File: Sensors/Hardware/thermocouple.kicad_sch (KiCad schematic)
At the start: 8 parts, among them U7 MAX31856

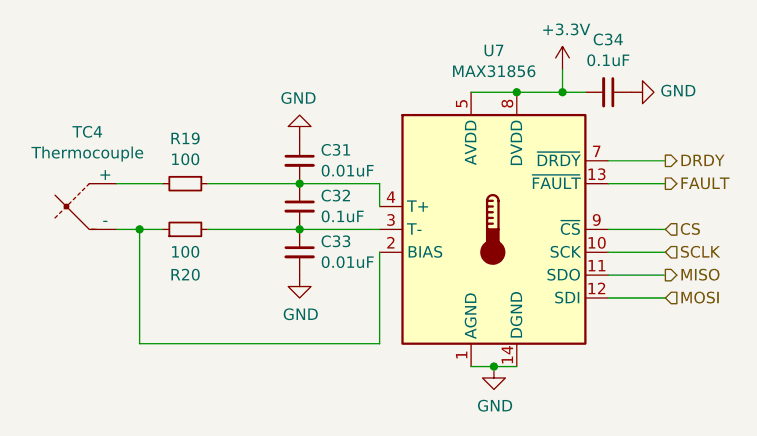
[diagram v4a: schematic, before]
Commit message: added 10V rail, moved to boosts sheet
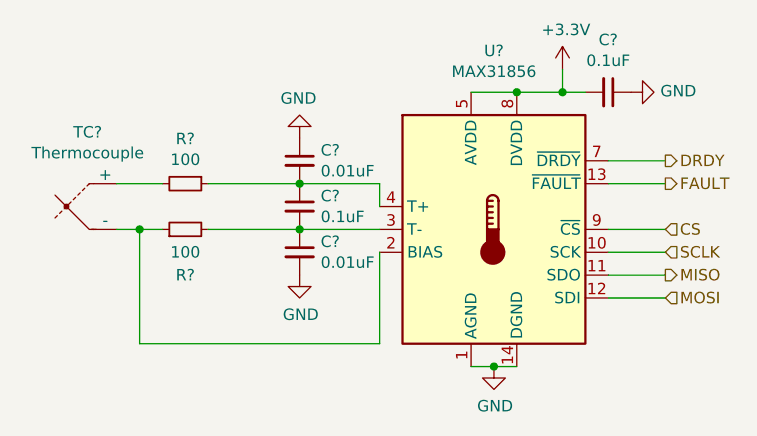
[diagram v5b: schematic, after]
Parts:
- renumbered C34 to C?, C32 to C?, C31 to C?, C33 to C?, R19 to R?, R20 to R?, TC4 to TC?, U7 to U?
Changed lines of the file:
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@@
   (symbol (lib_id "Sensor_Temperature:MAX31856") (at 95.25 73.66 0)
     (in_bom yes) (on_board yes)
-    (property "Reference" "U7" (id 0) (at 95.25 53.8226 0))
+    (property "Reference" "U?" (id 0) (at 95.25 53.8226 0))
     (property "Value" "MAX31856" (id 1) (at 95.25 56.134 0))
     (property "Footprint" "Package_SO:TSSOP-14_4.4x5mm_P0.65mm" (id 2) (at 99.06 87.63 0)
@@
   (symbol (lib_id "power:GND") (at 95.25 88.9 0)
     (in_bom yes) (on_board yes)
-    (property "Reference" "#PWR053" (id 0) (at 95.25 95.25 0)
+    (property "Reference" "#PWR?" (id 0) (at 95.25 95.25 0)
       (effects (font (size 1.27 1.27)) hide)
     )
@@
   (symbol (lib_id "analogue-cache:+3.3V") (at 102.87 55.88 0)
     (in_bom yes) (on_board yes)
-    (property "Reference" "#PWR054" (id 0) (at 102.87 59.69 0)
+    (property "Reference" "#PWR?" (id 0) (at 102.87 59.69 0)
       (effects (font (size 1.27 1.27)) hide)
     )
@@
   (symbol (lib_id "Device:C_Small") (at 107.95 58.42 270)
     (in_bom yes) (on_board yes)
-    (property "Reference" "C34" (id 0) (at 107.95 52.6034 90))
+    (property "Reference" "C?" (id 0) (at 107.95 52.6034 90))
     (property "Value" "0.1uF" (id 1) (at 107.95 54.9148 90))
     (property "Footprint" "Capacitor_SMD:C_0603_1608Metric" (id 2) (at 107.95 58.42 0)
@@
   (symbol (lib_id "power:GND") (at 110.49 58.42 90)
     (in_bom yes) (on_board yes)
-    (property "Reference" "#PWR055" (id 0) (at 116.84 58.42 0)
+    (property "Reference" "#PWR?" (id 0) (at 116.84 58.42 0)
       (effects (font (size 1.27 1.27)) hide)
     )
@@
   (symbol (lib_id "Device:Thermocouple") (at 50.8 71.12 0)
     (in_bom yes) (on_board yes)
-    (property "Reference" "TC4" (id 0) (at 50.1142 62.865 0))
+    (property "Reference" "TC?" (id 0) (at 50.1142 62.865 0))
     (property "Value" "Thermocouple" (id 1) (at 50.1142 65.1764 0))
     (property "Footprint" "TerminalBlock_TE-Connectivity:TerminalBlock_TE_282834-2_1x02_P2.54mm_Horizontal" (id 2) (at 36.195 69.85 0)
@@
   (symbol (lib_id "Device:R_Small") (at 60.96 68.58 270)
     (in_bom yes) (on_board yes)
-    (property "Reference" "R19" (id 0) (at 60.96 63.6016 90))
+    (property "Reference" "R?" (id 0) (at 60.96 63.6016 90))
     (property "Value" "100" (id 1) (at 60.96 65.913 90))
     (property "Footprint" "Resistor_SMD:R_0603_1608Metric" (id 2) (at 60.96 68.58 0)
@@
   (symbol (lib_id "Device:R_Small") (at 60.96 73.66 90)
     (in_bom yes) (on_board yes)
-    (property "Reference" "R20" (id 0) (at 60.96 78.74 90))
+    (property "Reference" "R?" (id 0) (at 60.96 78.74 90))
     (property "Value" "100" (id 1) (at 60.96 76.2 90))
     (property "Footprint" "Resistor_SMD:R_0603_1608Metric" (id 2) (at 60.96 73.66 0)
@@
   (symbol (lib_id "Device:C_Small") (at 73.66 71.12 0)
     (in_bom yes) (on_board yes)
-    (property "Reference" "C32" (id 0) (at 75.9968 69.9516 0)
+    (property "Reference" "C?" (id 0) (at 75.9968 69.9516 0)
       (effects (font (size 1.27 1.27)) (justify left))
     )
@@
   (symbol (lib_id "Device:C_Small") (at 73.66 66.04 0)
     (in_bom yes) (on_board yes)
-    (property "Reference" "C31" (id 0) (at 75.9968 64.8716 0)
+    (property "Reference" "C?" (id 0) (at 75.9968 64.8716 0)
       (effects (font (size 1.27 1.27)) (justify left))
     )
@@
   (symbol (lib_id "Device:C_Small") (at 73.66 76.2 0)
     (in_bom yes) (on_board yes)
-    (property "Reference" "C33" (id 0) (at 75.9968 75.0316 0)
+    (property "Reference" "C?" (id 0) (at 75.9968 75.0316 0)
       (effects (font (size 1.27 1.27)) (justify left))
     )
@@
   (symbol (lib_id "power:GND") (at 73.66 78.74 0)
     (in_bom yes) (on_board yes)
-    (property "Reference" "#PWR052" (id 0) (at 73.66 85.09 0)
+    (property "Reference" "#PWR?" (id 0) (at 73.66 85.09 0)
       (effects (font (size 1.27 1.27)) hide)
     )
@@
   (symbol (lib_id "power:GND") (at 73.66 63.5 180)
     (in_bom yes) (on_board yes)
-    (property "Reference" "#PWR051" (id 0) (at 73.66 57.15 0)
+    (property "Reference" "#PWR?" (id 0) (at 73.66 57.15 0)
       (effects (font (size 1.27 1.27)) hide)
     )

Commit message: fp assignments
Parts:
- C19, C20, C21, C22: renamed from C?; footprint Capacitor_SMD:C_0603_1608Metric -> Capacitor_SMD:C_0402_1005Metric
- R10, R11: renamed from R?; footprint Resistor_SMD:R_0603_1608Metric -> Resistor_SMD:R_0402_1005Metric
- gave numbers to parts that had none: 2
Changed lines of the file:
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@@
   (symbol (lib_id "Sensor_Temperature:MAX31856") (at 95.25 73.66 0)
     (in_bom yes) (on_board yes)
-    (property "Reference" "U?" (id 0) (at 95.25 53.8226 0))
+    (property "Reference" "U3" (id 0) (at 95.25 53.8226 0))
     (property "Value" "MAX31856" (id 1) (at 95.25 56.134 0))
     (property "Footprint" "Package_SO:TSSOP-14_4.4x5mm_P0.65mm" (id 2) (at 99.06 87.63 0)
@@
   (symbol (lib_id "power:GND") (at 95.25 88.9 0)
     (in_bom yes) (on_board yes)
-    (property "Reference" "#PWR?" (id 0) (at 95.25 95.25 0)
+    (property "Reference" "#PWR034" (id 0) (at 95.25 95.25 0)
       (effects (font (size 1.27 1.27)) hide)
     )
@@
   (symbol (lib_id "analogue-cache:+3.3V") (at 102.87 55.88 0)
     (in_bom yes) (on_board yes)
-    (property "Reference" "#PWR?" (id 0) (at 102.87 59.69 0)
+    (property "Reference" "#PWR035" (id 0) (at 102.87 59.69 0)
       (effects (font (size 1.27 1.27)) hide)
     )
@@
   (symbol (lib_id "Device:C_Small") (at 107.95 58.42 270)
     (in_bom yes) (on_board yes)
-    (property "Reference" "C?" (id 0) (at 107.95 52.6034 90))
+    (property "Reference" "C22" (id 0) (at 107.95 52.6034 90))
     (property "Value" "0.1uF" (id 1) (at 107.95 54.9148 90))
-    (property "Footprint" "Capacitor_SMD:C_0603_1608Metric" (id 2) (at 107.95 58.42 0)
+    (property "Footprint" "Capacitor_SMD:C_0402_1005Metric" (id 2) (at 107.95 58.42 0)
       (effects (font (size 1.27 1.27)) hide)
     )
@@
   (symbol (lib_id "power:GND") (at 110.49 58.42 90)
     (in_bom yes) (on_board yes)
-    (property "Reference" "#PWR?" (id 0) (at 116.84 58.42 0)
+    (property "Reference" "#PWR036" (id 0) (at 116.84 58.42 0)
       (effects (font (size 1.27 1.27)) hide)
     )
@@
   (symbol (lib_id "Device:Thermocouple") (at 50.8 71.12 0)
     (in_bom yes) (on_board yes)
-    (property "Reference" "TC?" (id 0) (at 50.1142 62.865 0))
+    (property "Reference" "TC2" (id 0) (at 50.1142 62.865 0))
     (property "Value" "Thermocouple" (id 1) (at 50.1142 65.1764 0))
     (property "Footprint" "TerminalBlock_TE-Connectivity:TerminalBlock_TE_282834-2_1x02_P2.54mm_Horizontal" (id 2) (at 36.195 69.85 0)
@@
   (symbol (lib_id "Device:R_Small") (at 60.96 68.58 270)
     (in_bom yes) (on_board yes)
-    (property "Reference" "R?" (id 0) (at 60.96 63.6016 90))
+    (property "Reference" "R10" (id 0) (at 60.96 63.6016 90))
     (property "Value" "100" (id 1) (at 60.96 65.913 90))
-    (property "Footprint" "Resistor_SMD:R_0603_1608Metric" (id 2) (at 60.96 68.58 0)
+    (property "Footprint" "Resistor_SMD:R_0402_1005Metric" (id 2) (at 60.96 68.58 0)
       (effects (font (size 1.27 1.27)) hide)
     )
@@
   (symbol (lib_id "Device:R_Small") (at 60.96 73.66 90)
     (in_bom yes) (on_board yes)
-    (property "Reference" "R?" (id 0) (at 60.96 78.74 90))
+    (property "Reference" "R11" (id 0) (at 60.96 78.74 90))
     (property "Value" "100" (id 1) (at 60.96 76.2 90))
-    (property "Footprint" "Resistor_SMD:R_0603_1608Metric" (id 2) (at 60.96 73.66 0)
+    (property "Footprint" "Resistor_SMD:R_0402_1005Metric" (id 2) (at 60.96 73.66 0)
       (effects (font (size 1.27 1.27)) hide)
     )
@@
   (symbol (lib_id "Device:C_Small") (at 73.66 71.12 0)
     (in_bom yes) (on_board yes)
-    (property "Reference" "C?" (id 0) (at 75.9968 69.9516 0)
+    (property "Reference" "C20" (id 0) (at 75.9968 69.9516 0)
       (effects (font (size 1.27 1.27)) (justify left))
     )
@@
       (effects (font (size 1.27 1.27)) (justify left))
     )
-    (property "Footprint" "Capacitor_SMD:C_0603_1608Metric" (id 2) (at 73.66 71.12 0)
+    (property "Footprint" "Capacitor_SMD:C_0402_1005Metric" (id 2) (at 73.66 71.12 0)
       (effects (font (size 1.27 1.27)) hide)
     )
@@
   (symbol (lib_id "Device:C_Small") (at 73.66 66.04 0)
     (in_bom yes) (on_board yes)
-    (property "Reference" "C?" (id 0) (at 75.9968 64.8716 0)
+    (property "Reference" "C19" (id 0) (at 75.9968 64.8716 0)
       (effects (font (size 1.27 1.27)) (justify left))
     )
@@
       (effects (font (size 1.27 1.27)) (justify left))
     )
-    (property "Footprint" "Capacitor_SMD:C_0603_1608Metric" (id 2) (at 73.66 66.04 0)
+    (property "Footprint" "Capacitor_SMD:C_0402_1005Metric" (id 2) (at 73.66 66.04 0)
       (effects (font (size 1.27 1.27)) hide)
     )
@@
   (symbol (lib_id "Device:C_Small") (at 73.66 76.2 0)
     (in_bom yes) (on_board yes)
-    (property "Reference" "C?" (id 0) (at 75.9968 75.0316 0)
+    (property "Reference" "C21" (id 0) (at 75.9968 75.0316 0)
       (effects (font (size 1.27 1.27)) (justify left))
     )
@@
       (effects (font (size 1.27 1.27)) (justify left))
     )
-    (property "Footprint" "Capacitor_SMD:C_0603_1608Metric" (id 2) (at 73.66 76.2 0)
+    (property "Footprint" "Capacitor_SMD:C_0402_1005Metric" (id 2) (at 73.66 76.2 0)
       (effects (font (size 1.27 1.27)) hide)
     )
@@
   (symbol (lib_id "power:GND") (at 73.66 78.74 0)
     (in_bom yes) (on_board yes)
-    (property "Reference" "#PWR?" (id 0) (at 73.66 85.09 0)
+    (property "Reference" "#PWR033" (id 0) (at 73.66 85.09 0)
       (effects (font (size 1.27 1.27)) hide)
     )
@@
   (symbol (lib_id "power:GND") (at 73.66 63.5 180)
     (in_bom yes) (on_board yes)
-    (property "Reference" "#PWR?" (id 0) (at 73.66 57.15 0)
+    (property "Reference" "#PWR032" (id 0) (at 73.66 57.15 0)
       (effects (font (size 1.27 1.27)) hide)
     )

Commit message: update (tps and filters)
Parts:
- renumbered C19 to C15, C20 to C16, C21 to C17, C22 to C18, R10 to R8, R11 to R9, TC2 to TC1, U3 to U2
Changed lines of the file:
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@@
   (symbol (lib_id "Sensor_Temperature:MAX31856") (at 95.25 73.66 0)
     (in_bom yes) (on_board yes)
-    (property "Reference" "U3" (id 0) (at 95.25 53.8226 0))
+    (property "Reference" "U2" (id 0) (at 95.25 53.8226 0))
     (property "Value" "MAX31856" (id 1) (at 95.25 56.134 0))
     (property "Footprint" "Package_SO:TSSOP-14_4.4x5mm_P0.65mm" (id 2) (at 99.06 87.63 0)
@@
   (symbol (lib_id "power:GND") (at 95.25 88.9 0)
     (in_bom yes) (on_board yes)
-    (property "Reference" "#PWR034" (id 0) (at 95.25 95.25 0)
+    (property "Reference" "#PWR044" (id 0) (at 95.25 95.25 0)
       (effects (font (size 1.27 1.27)) hide)
     )
@@
   (symbol (lib_id "analogue-cache:+3.3V") (at 102.87 55.88 0)
     (in_bom yes) (on_board yes)
-    (property "Reference" "#PWR035" (id 0) (at 102.87 59.69 0)
+    (property "Reference" "#PWR045" (id 0) (at 102.87 59.69 0)
       (effects (font (size 1.27 1.27)) hide)
     )
@@
   (symbol (lib_id "Device:C_Small") (at 107.95 58.42 270)
     (in_bom yes) (on_board yes)
-    (property "Reference" "C22" (id 0) (at 107.95 52.6034 90))
+    (property "Reference" "C18" (id 0) (at 107.95 52.6034 90))
     (property "Value" "0.1uF" (id 1) (at 107.95 54.9148 90))
     (property "Footprint" "Capacitor_SMD:C_0402_1005Metric" (id 2) (at 107.95 58.42 0)
@@
   (symbol (lib_id "power:GND") (at 110.49 58.42 90)
     (in_bom yes) (on_board yes)
-    (property "Reference" "#PWR036" (id 0) (at 116.84 58.42 0)
+    (property "Reference" "#PWR046" (id 0) (at 116.84 58.42 0)
       (effects (font (size 1.27 1.27)) hide)
     )
@@
   (symbol (lib_id "Device:Thermocouple") (at 50.8 71.12 0)
     (in_bom yes) (on_board yes)
-    (property "Reference" "TC2" (id 0) (at 50.1142 62.865 0))
+    (property "Reference" "TC1" (id 0) (at 50.1142 62.865 0))
     (property "Value" "Thermocouple" (id 1) (at 50.1142 65.1764 0))
     (property "Footprint" "TerminalBlock_TE-Connectivity:TerminalBlock_TE_282834-2_1x02_P2.54mm_Horizontal" (id 2) (at 36.195 69.85 0)
@@
   (symbol (lib_id "Device:R_Small") (at 60.96 68.58 270)
     (in_bom yes) (on_board yes)
-    (property "Reference" "R10" (id 0) (at 60.96 63.6016 90))
+    (property "Reference" "R8" (id 0) (at 60.96 63.6016 90))
     (property "Value" "100" (id 1) (at 60.96 65.913 90))
     (property "Footprint" "Resistor_SMD:R_0402_1005Metric" (id 2) (at 60.96 68.58 0)
@@
   (symbol (lib_id "Device:R_Small") (at 60.96 73.66 90)
     (in_bom yes) (on_board yes)
-    (property "Reference" "R11" (id 0) (at 60.96 78.74 90))
+    (property "Reference" "R9" (id 0) (at 60.96 78.74 90))
     (property "Value" "100" (id 1) (at 60.96 76.2 90))
     (property "Footprint" "Resistor_SMD:R_0402_1005Metric" (id 2) (at 60.96 73.66 0)
@@
   (symbol (lib_id "Device:C_Small") (at 73.66 71.12 0)
     (in_bom yes) (on_board yes)
-    (property "Reference" "C20" (id 0) (at 75.9968 69.9516 0)
+    (property "Reference" "C16" (id 0) (at 75.9968 69.9516 0)
       (effects (font (size 1.27 1.27)) (justify left))
     )
@@
   (symbol (lib_id "Device:C_Small") (at 73.66 66.04 0)
     (in_bom yes) (on_board yes)
-    (property "Reference" "C19" (id 0) (at 75.9968 64.8716 0)
+    (property "Reference" "C15" (id 0) (at 75.9968 64.8716 0)
       (effects (font (size 1.27 1.27)) (justify left))
     )
@@
   (symbol (lib_id "Device:C_Small") (at 73.66 76.2 0)
     (in_bom yes) (on_board yes)
-    (property "Reference" "C21" (id 0) (at 75.9968 75.0316 0)
+    (property "Reference" "C17" (id 0) (at 75.9968 75.0316 0)
       (effects (font (size 1.27 1.27)) (justify left))
     )
@@
   (symbol (lib_id "power:GND") (at 73.66 78.74 0)
     (in_bom yes) (on_board yes)
-    (property "Reference" "#PWR033" (id 0) (at 73.66 85.09 0)
+    (property "Reference" "#PWR043" (id 0) (at 73.66 85.09 0)
       (effects (font (size 1.27 1.27)) hide)
     )
@@
   (symbol (lib_id "power:GND") (at 73.66 63.5 180)
     (in_bom yes) (on_board yes)
-    (property "Reference" "#PWR032" (id 0) (at 73.66 57.15 0)
+    (property "Reference" "#PWR042" (id 0) (at 73.66 57.15 0)
       (effects (font (size 1.27 1.27)) hide)
     )

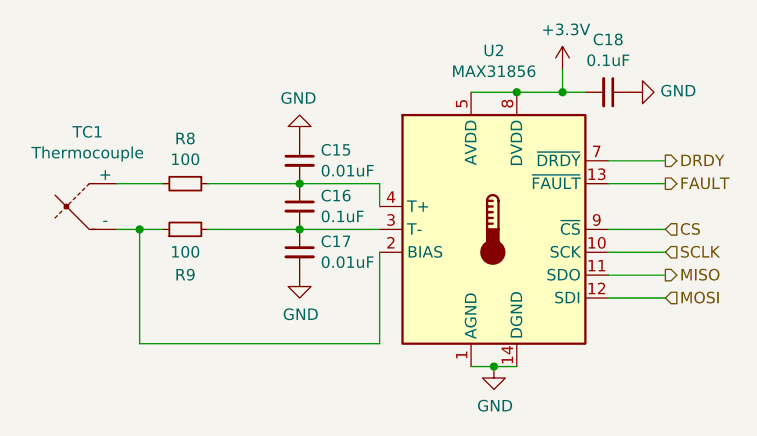
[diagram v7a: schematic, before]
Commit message: redimensioning to 120x50mm
also finished tps
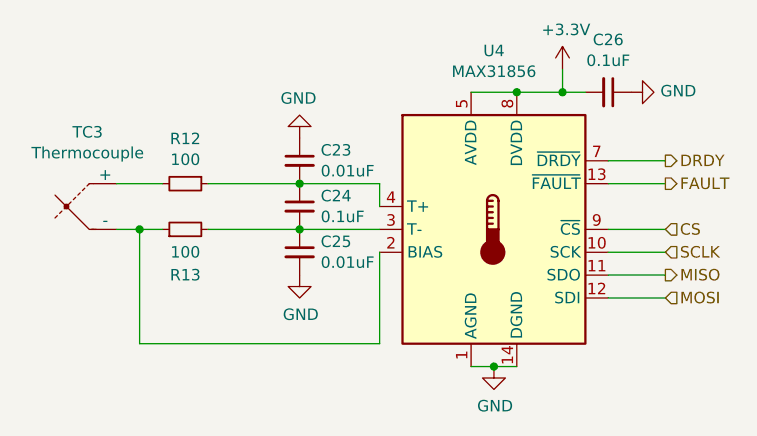
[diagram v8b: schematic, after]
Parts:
- renumbered C15 to C23, C16 to C24, C17 to C25, C18 to C26, R8 to R12, R9 to R13, TC1 to TC3, U2 to U4
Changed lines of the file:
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@@
   (symbol (lib_id "Sensor_Temperature:MAX31856") (at 95.25 73.66 0)
     (in_bom yes) (on_board yes)
-    (property "Reference" "U2" (id 0) (at 95.25 53.8226 0))
+    (property "Reference" "U4" (id 0) (at 95.25 53.8226 0))
     (property "Value" "MAX31856" (id 1) (at 95.25 56.134 0))
     (property "Footprint" "Package_SO:TSSOP-14_4.4x5mm_P0.65mm" (id 2) (at 99.06 87.63 0)
@@
   (symbol (lib_id "Device:C_Small") (at 107.95 58.42 270)
     (in_bom yes) (on_board yes)
-    (property "Reference" "C18" (id 0) (at 107.95 52.6034 90))
+    (property "Reference" "C26" (id 0) (at 107.95 52.6034 90))
     (property "Value" "0.1uF" (id 1) (at 107.95 54.9148 90))
     (property "Footprint" "Capacitor_SMD:C_0402_1005Metric" (id 2) (at 107.95 58.42 0)
@@
   (symbol (lib_id "Device:Thermocouple") (at 50.8 71.12 0)
     (in_bom yes) (on_board yes)
-    (property "Reference" "TC1" (id 0) (at 50.1142 62.865 0))
+    (property "Reference" "TC3" (id 0) (at 50.1142 62.865 0))
     (property "Value" "Thermocouple" (id 1) (at 50.1142 65.1764 0))
     (property "Footprint" "TerminalBlock_TE-Connectivity:TerminalBlock_TE_282834-2_1x02_P2.54mm_Horizontal" (id 2) (at 36.195 69.85 0)
@@
   (symbol (lib_id "Device:R_Small") (at 60.96 68.58 270)
     (in_bom yes) (on_board yes)
-    (property "Reference" "R8" (id 0) (at 60.96 63.6016 90))
+    (property "Reference" "R12" (id 0) (at 60.96 63.6016 90))
     (property "Value" "100" (id 1) (at 60.96 65.913 90))
     (property "Footprint" "Resistor_SMD:R_0402_1005Metric" (id 2) (at 60.96 68.58 0)
@@
   (symbol (lib_id "Device:R_Small") (at 60.96 73.66 90)
     (in_bom yes) (on_board yes)
-    (property "Reference" "R9" (id 0) (at 60.96 78.74 90))
+    (property "Reference" "R13" (id 0) (at 60.96 78.74 90))
     (property "Value" "100" (id 1) (at 60.96 76.2 90))
     (property "Footprint" "Resistor_SMD:R_0402_1005Metric" (id 2) (at 60.96 73.66 0)
@@
   (symbol (lib_id "Device:C_Small") (at 73.66 71.12 0)
     (in_bom yes) (on_board yes)
-    (property "Reference" "C16" (id 0) (at 75.9968 69.9516 0)
+    (property "Reference" "C24" (id 0) (at 75.9968 69.9516 0)
       (effects (font (size 1.27 1.27)) (justify left))
     )
@@
   (symbol (lib_id "Device:C_Small") (at 73.66 66.04 0)
     (in_bom yes) (on_board yes)
-    (property "Reference" "C15" (id 0) (at 75.9968 64.8716 0)
+    (property "Reference" "C23" (id 0) (at 75.9968 64.8716 0)
       (effects (font (size 1.27 1.27)) (justify left))
     )
@@
   (symbol (lib_id "Device:C_Small") (at 73.66 76.2 0)
     (in_bom yes) (on_board yes)
-    (property "Reference" "C17" (id 0) (at 75.9968 75.0316 0)
+    (property "Reference" "C25" (id 0) (at 75.9968 75.0316 0)
       (effects (font (size 1.27 1.27)) (justify left))
     )
